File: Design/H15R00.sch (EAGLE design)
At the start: 21 parts, among them P1 HEXABIT_17.32_NO_P3_P6, U1 STM32F091CBU6, X1 XTALL_CSTCE8M00G52

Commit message: Finished schematics
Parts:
- added AO: 1751248, Hexabitz:CON-PHOENIX-350_1751248
- added C10, C11: 100nF, Hexabitz:C-0603
- added C12, C13: 100pF, Hexabitz:C-0603
- added C14, C15: 10pF, Hexabitz:C-0603
- added C16: 20nF, Hexabitz:C-0603
- added C17: 150pF, Hexabitz:C-0603
- added PWR: 1751251, con-phoenix-350:1751251
- added R4: 71.5R, Hexabitz:R-0603
- added R5: 24.9K, Hexabitz:R-0603
- added R6: 8.25K, Hexabitz:R-0603
- added R7: 12.4K, Hexabitz:R-0603
- added U2: OPA188, Hexabitz:OPA188AIDBVR
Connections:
- net UART1_RX renamed UART1_RX*
- net UART1_TX renamed UART1_TX*
- net UART2_RX renamed UART2_RX*
- net UART2_TX renamed UART2_TX*
- removed net UART6_RX: U1.PA5
- removed net UART6_TX: U1.PA4
- new net +15V: C11.1, C13.1, C14.1, PWR-3.K, U2.V+
- new net -15V: C10.1, C12.1, C15.1, PWR-1.K, U2.V-
- new net AGND: AO-2.K, C10.2, C12.2, C14.2, C15.2, C16.2, PWR-2.K, R7.2
- new net DAC_OUT: U1.PA4, U2.IN+
- new net N$1: AO-1.K, C16.1, R4.1
- new net N$10: R5.1
- new net N$11: P1.SU1
- new net N$12: P1.SU2
- new net N$13: P1.SU4
- new net N$14: P1.SD5
- new net N$15: P1.SD1
- new net N$16: P1.SD2
- new net N$17: P1.SD4
- new net N$18: P1.SU5
- new net N$2: C17.2, R4.2, U2.OUT
- new net N$8: C17.1, R5.2, R6.1, R7.1, U2.IN-
- new net VCC: R6.2
- net VSSA: now also C11.2, C13.2
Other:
- note added: "Analog Output +/-10V"
- note added: "Analog Power"

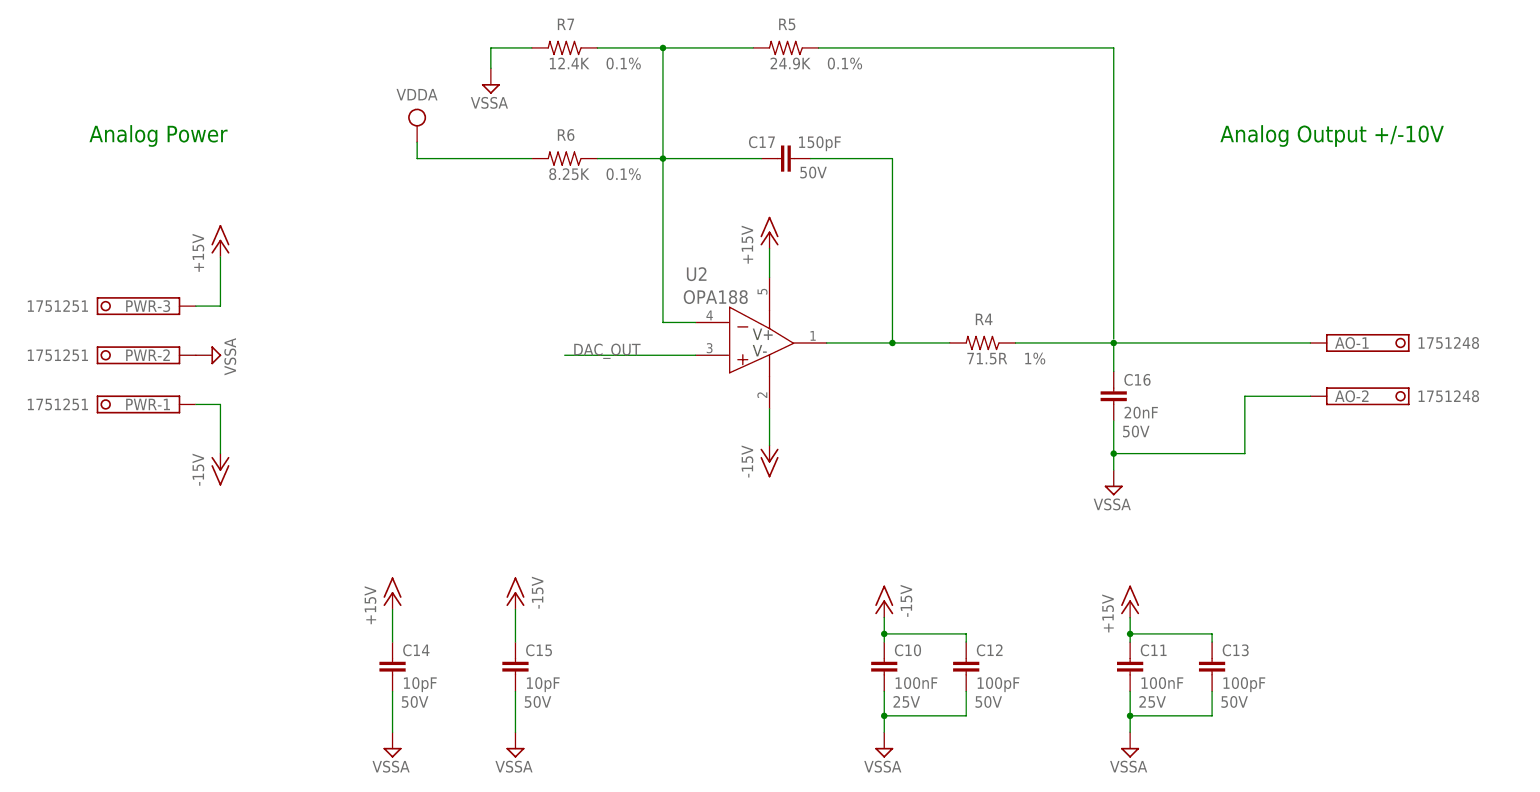
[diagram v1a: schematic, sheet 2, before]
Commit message: Placed all components Routed analog part and most digital Added VSSA polygon
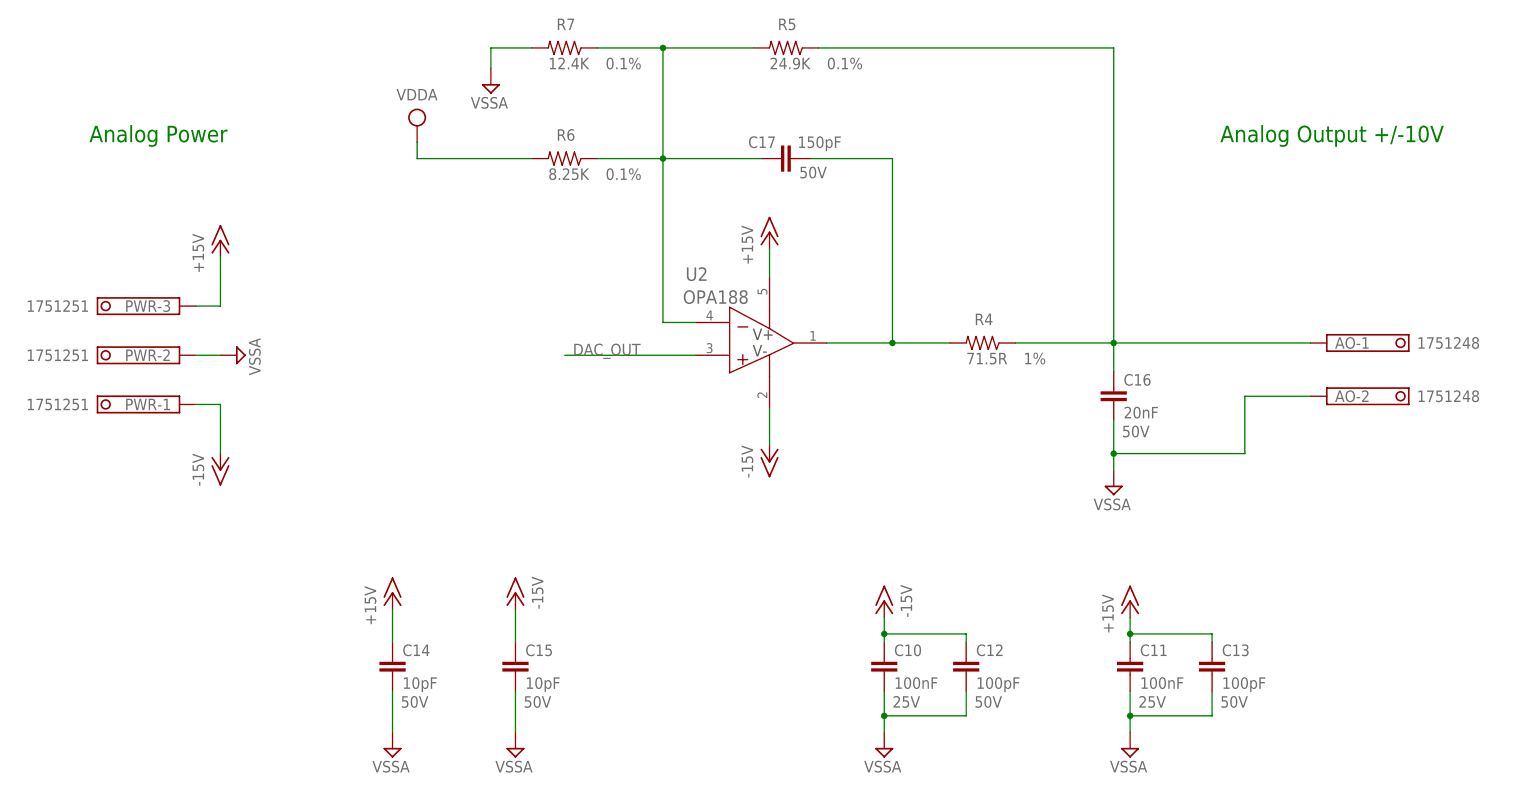
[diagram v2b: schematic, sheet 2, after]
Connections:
- removed net AGND: AO-2.K, C10.2, C12.2, C14.2, C15.2, C16.2, PWR-2.K, R7.2
- removed net N$10: R5.1
- removed net N$11: P1.SU1
- removed net N$12: P1.SU2
- removed net N$13: P1.SU4
- removed net N$14: P1.SD5
- removed net N$15: P1.SD1
- removed net N$16: P1.SD2
- removed net N$17: P1.SD4
- removed net N$18: P1.SU5
- removed net VCC: R6.2
- net N$1: now also R5.1
- net UART1_RX*: now also P1.SD5
- net UART1_TX*: now also P1.SU5
- net UART2_RX*: now also P1.SD2
- net UART2_TX*: now also P1.SU2
- net UART3_RX: now also P1.SD4
- net UART3_TX: now also P1.SU4
- net UART5_RX: now also P1.SD1
- net UART5_TX: now also P1.SU1
- net VDDA: now also R6.2
- net VSSA: now also AO-2.K, C10.2, C12.2, C14.2, C15.2, C16.2, PWR-2.K, R7.2
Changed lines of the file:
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@@
 <setting verticaltext="up"/>
 </settings>
-<grid distance="50" unitdist="mil" unit="mil" style="lines" multiple="1" display="no" altdistance="0.01" altunitdist="inch" altunit="inch"/>
+<grid distance="25" unitdist="mil" unit="mil" style="lines" multiple="1" display="no" altdistance="0.01" altunitdist="inch" altunit="inch"/>
 <layers>
 <layer number="1" name="Top" color="4" fill="1" visible="no" active="no"/>
@@
 <label x="191.77" y="170.18" size="1.778" layer="95"/>
 </segment>
+<segment>
+<pinref part="P1" gate="G$1" pin="SU1"/>
+<wire x1="68.58" y1="172.72" x2="82.55" y2="172.72" width="0.1524" layer="91"/>
+<label x="69.85" y="172.72" size="1.778" layer="95"/>
+</segment>
 </net>
 <net name="UART5_RX" class="0">
@@
 <label x="191.77" y="167.64" size="1.778" layer="95"/>
 </segment>
+<segment>
+<pinref part="P1" gate="G$1" pin="SD1"/>
+<wire x1="68.58" y1="137.16" x2="82.55" y2="137.16" width="0.1524" layer="91"/>
+<label x="69.85" y="137.16" size="1.778" layer="95"/>
+</segment>
 </net>
 <net name="UART3_TX" class="0">
@@
 <wire x1="191.77" y1="152.4" x2="205.74" y2="152.4" width="0.1524" layer="91"/>
 <label x="191.77" y="152.4" size="1.778" layer="95"/>
+</segment>
+<segment>
+<pinref part="P1" gate="G$1" pin="SU4"/>
+<wire x1="68.58" y1="157.48" x2="82.55" y2="157.48" width="0.1524" layer="91"/>
 <label x="69.85" y="157.48" size="1.778" layer="95"/>
 </segment>
@@
 <label x="121.92" y="154.94" size="1.778" layer="95"/>
 <pinref part="U1" gate="G$1" pin="PA9"/>
+</segment>
+<segment>
+<pinref part="P1" gate="G$1" pin="SU5"/>
+<wire x1="68.58" y1="152.4" x2="82.55" y2="152.4" width="0.1524" layer="91"/>
 <label x="69.85" y="152.4" size="1.778" layer="95"/>
 </segment>
@@
 <wire x1="191.77" y1="149.86" x2="205.74" y2="149.86" width="0.1524" layer="91"/>
 <label x="191.77" y="149.86" size="1.778" layer="95"/>
+</segment>
+<segment>
+<pinref part="P1" gate="G$1" pin="SD4"/>
+<wire x1="68.58" y1="121.92" x2="82.55" y2="121.92" width="0.1524" layer="91"/>
 <label x="69.85" y="121.92" size="1.778" layer="95"/>
 </segment>
@@
 <label x="121.92" y="152.4" size="1.778" layer="95"/>
 <pinref part="U1" gate="G$1" pin="PA10"/>
+</segment>
+<segment>
+<pinref part="P1" gate="G$1" pin="SD5"/>
+<wire x1="68.58" y1="116.84" x2="82.55" y2="116.84" width="0.1524" layer="91"/>
 <label x="69.85" y="116.84" size="1.778" layer="95"/>
 </segment>
@@
 <wire x1="135.89" y1="172.72" x2="121.92" y2="172.72" width="0.1524" layer="91"/>
 <label x="121.92" y="172.72" size="1.778" layer="95"/>
+</segment>
+<segment>
+<pinref part="P1" gate="G$1" pin="SU2"/>
+<wire x1="68.58" y1="167.64" x2="82.55" y2="167.64" width="0.1524" layer="91"/>
 <label x="69.85" y="167.64" size="1.778" layer="95"/>
 </segment>
@@
 <wire x1="135.89" y1="170.18" x2="121.92" y2="170.18" width="0.1524" layer="91"/>
 <label x="121.92" y="170.18" size="1.778" layer="95"/>
+</segment>
+<segment>
+<pinref part="P1" gate="G$1" pin="SD2"/>
+<wire x1="68.58" y1="132.08" x2="82.55" y2="132.08" width="0.1524" layer="91"/>
 <label x="69.85" y="132.08" size="1.778" layer="95"/>
 </segment>
@@
 <wire x1="135.89" y1="177.8" x2="121.92" y2="177.8" width="0.1524" layer="91"/>
 <label x="121.92" y="177.8" size="1.778" layer="95"/>
-<label x="69.85" y="172.72" size="1.778" layer="95"/>
 </segment>
 </net>
@@
 <wire x1="135.89" y1="175.26" x2="121.92" y2="175.26" width="0.1524" layer="91"/>
 <label x="121.92" y="175.26" size="1.778" layer="95"/>
-<label x="69.85" y="137.16" size="1.778" layer="95"/>
 </segment>
 </net>
@@
 </segment>
 </net>
-<net name="N$11" class="0">
-<segment>
-<pinref part="P1" gate="G$1" pin="SU1"/>
-<wire x1="68.58" y1="172.72" x2="82.55" y2="172.72" width="0.1524" layer="91"/>
-</segment>
-</net>
-<net name="N$12" class="0">
-<segment>
-<pinref part="P1" gate="G$1" pin="SU2"/>
-<wire x1="68.58" y1="167.64" x2="82.55" y2="167.64" width="0.1524" layer="91"/>
-</segment>
-</net>
-<net name="N$13" class="0">
-<segment>
-<pinref part="P1" gate="G$1" pin="SU4"/>
-<wire x1="68.58" y1="157.48" x2="82.55" y2="157.48" width="0.1524" layer="91"/>
-</segment>
-</net>
-<net name="N$15" class="0">
-<segment>
-<pinref part="P1" gate="G$1" pin="SD1"/>
-<wire x1="68.58" y1="137.16" x2="82.55" y2="137.16" width="0.1524" layer="91"/>
-</segment>
-</net>
-<net name="N$16" class="0">
-<segment>
-<pinref part="P1" gate="G$1" pin="SD2"/>
-<wire x1="68.58" y1="132.08" x2="82.55" y2="132.08" width="0.1524" layer="91"/>
-</segment>
-</net>
-<net name="N$17" class="0">
-<segment>
-<pinref part="P1" gate="G$1" pin="SD4"/>
-<wire x1="68.58" y1="121.92" x2="82.55" y2="121.92" width="0.1524" layer="91"/>
-</segment>
-</net>
 <net name="DAC_OUT" class="0">
 <segment>
@@
 </segment>
 </net>
-<net name="N$14" class="0">
-<segment>
-<pinref part="P1" gate="G$1" pin="SD5"/>
-<wire x1="68.58" y1="116.84" x2="82.55" y2="116.84" width="0.1524" layer="91"/>
-</segment>
-</net>
-<net name="N$18" class="0">
-<segment>
-<pinref part="P1" gate="G$1" pin="SU5"/>
-<wire x1="68.58" y1="152.4" x2="82.55" y2="152.4" width="0.1524" layer="91"/>
-</segment>
-</net>
 </nets>
 </sheet>
@@
 <attribute name="VALUE" x="198.247" y="71.755" size="1.778" layer="96" rot="R180"/>
 </instance>
-<instance part="SUPPLY16" gate="G$1" x="53.34" y="134.62" smashed="yes" rot="R90">
-<attribute name="VALUE" x="55.245" y="137.287" size="1.778" layer="96" rot="R270"/>
+<instance part="SUPPLY16" gate="G$1" x="57.15" y="134.62" smashed="yes" rot="R90">
+<attribute name="VALUE" x="59.055" y="137.287" size="1.778" layer="96" rot="R270"/>
 </instance>
 <instance part="C11" gate="G$1" x="195.58" y="85.09" smashed="yes">
@@
 <junction x="195.58" y="78.74"/>
 </segment>
-</net>
-<net name="AGND" class="0">
+<segment>
+<pinref part="C16" gate="G$1" pin="2"/>
+<pinref part="SUPPLY20" gate="G$1" pin="AGND"/>
+<wire x1="193.04" y1="124.46" x2="193.04" y2="119.38" width="0.1524" layer="91"/>
+<pinref part="AO" gate="-2" pin="K"/>
+<wire x1="193.04" y1="119.38" x2="193.04" y2="116.84" width="0.1524" layer="91"/>
+<wire x1="223.52" y1="128.27" x2="213.36" y2="128.27" width="0.1524" layer="91"/>
+<wire x1="213.36" y1="128.27" x2="213.36" y2="119.38" width="0.1524" layer="91"/>
+<wire x1="213.36" y1="119.38" x2="193.04" y2="119.38" width="0.1524" layer="91"/>
+<junction x="193.04" y="119.38"/>
+</segment>
 <segment>
 <pinref part="PWR" gate="-2" pin="K"/>
 <pinref part="SUPPLY16" gate="G$1" pin="AGND"/>
+<wire x1="54.61" y1="134.62" x2="50.8" y2="134.62" width="0.1524" layer="91"/>
 </segment>
 <segment>
@@
 </segment>
 <segment>
-<pinref part="C16" gate="G$1" pin="2"/>
-<pinref part="SUPPLY20" gate="G$1" pin="AGND"/>
-<wire x1="193.04" y1="124.46" x2="193.04" y2="119.38" width="0.1524" layer="91"/>
-<pinref part="AO" gate="-2" pin="K"/>
-<wire x1="193.04" y1="119.38" x2="193.04" y2="116.84" width="0.1524" layer="91"/>
-<wire x1="223.52" y1="128.27" x2="213.36" y2="128.27" width="0.1524" layer="91"/>
-<wire x1="213.36" y1="128.27" x2="213.36" y2="119.38" width="0.1524" layer="91"/>
-<wire x1="213.36" y1="119.38" x2="193.04" y2="119.38" width="0.1524" layer="91"/>
-<junction x="193.04" y="119.38"/>
-</segment>
-<segment>
 <pinref part="R7" gate="G$1" pin="2"/>
 <pinref part="SUPPLY17" gate="G$1" pin="AGND"/>
@@
 <pinref part="AO" gate="-1" pin="K"/>
 <wire x1="223.52" y1="136.525" x2="193.04" y2="136.525" width="0.1524" layer="91"/>
-<pinref part="C16" gate="G$1" pin="1"/>
 <wire x1="193.04" y1="136.525" x2="177.8" y2="136.525" width="0.1524" layer="91"/>
-<wire x1="193.04" y1="132.08" x2="193.04" y2="136.525" width="0.1524" layer="91"/>
 <junction x="193.04" y="136.525"/>
 <pinref part="R4" gate="G$1" pin="1"/>
+<pinref part="R5" gate="G$1" pin="1"/>
+<wire x1="147.32" y1="182.245" x2="193.04" y2="182.245" width="0.1524" layer="91"/>
+<wire x1="193.04" y1="182.245" x2="193.04" y2="136.525" width="0.1524" layer="91"/>
+<pinref part="C16" gate="G$1" pin="1"/>
+<wire x1="193.04" y1="132.08" x2="193.04" y2="136.525" width="0.1524" layer="91"/>
 </segment>
 </net>
@@
 </segment>
 </net>
-<net name="N$10" class="0">
-<segment>
-<pinref part="R5" gate="G$1" pin="1"/>
-<wire x1="147.32" y1="182.245" x2="193.04" y2="182.245" width="0.1524" layer="91"/>
-<wire x1="193.04" y1="182.245" x2="193.04" y2="137.16" width="0.1524" layer="91"/>
-</segment>
-</net>
-<net name="VCC" class="0">
+<net name="VDDA" class="0">
 <segment>
 <pinref part="SUPPLY21" gate="G$1" pin="VCC"/>
@@
 </sheet>
 </sheets>
+<errors>
+</errors>
 </schematic>
 </drawing>
